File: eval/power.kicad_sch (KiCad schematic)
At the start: 33 parts, among them Q1 BSC0702LS, Q2 BSC0702LS, U2 LM5148RGYR, U3 INA180A3, U8 INA180A3

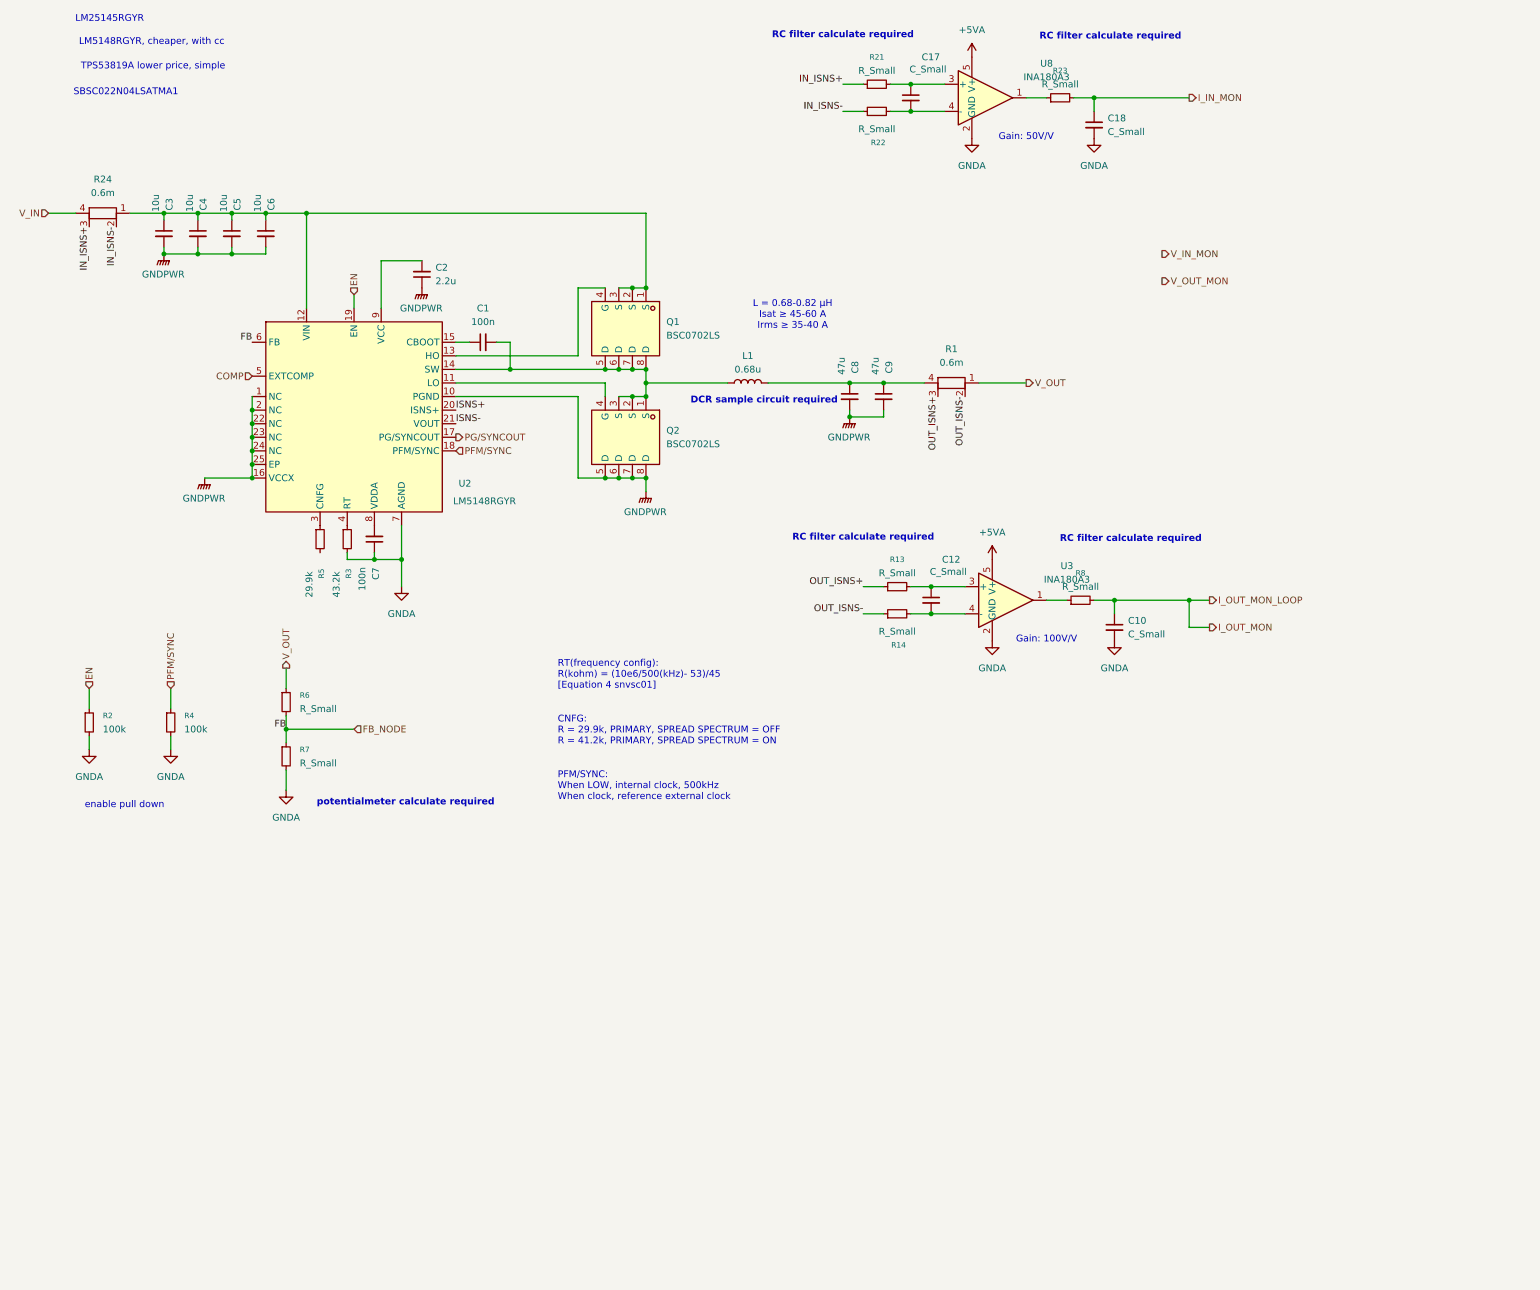
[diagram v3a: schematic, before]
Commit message: Complete first complete draft sch (add screen spi and back light cc)
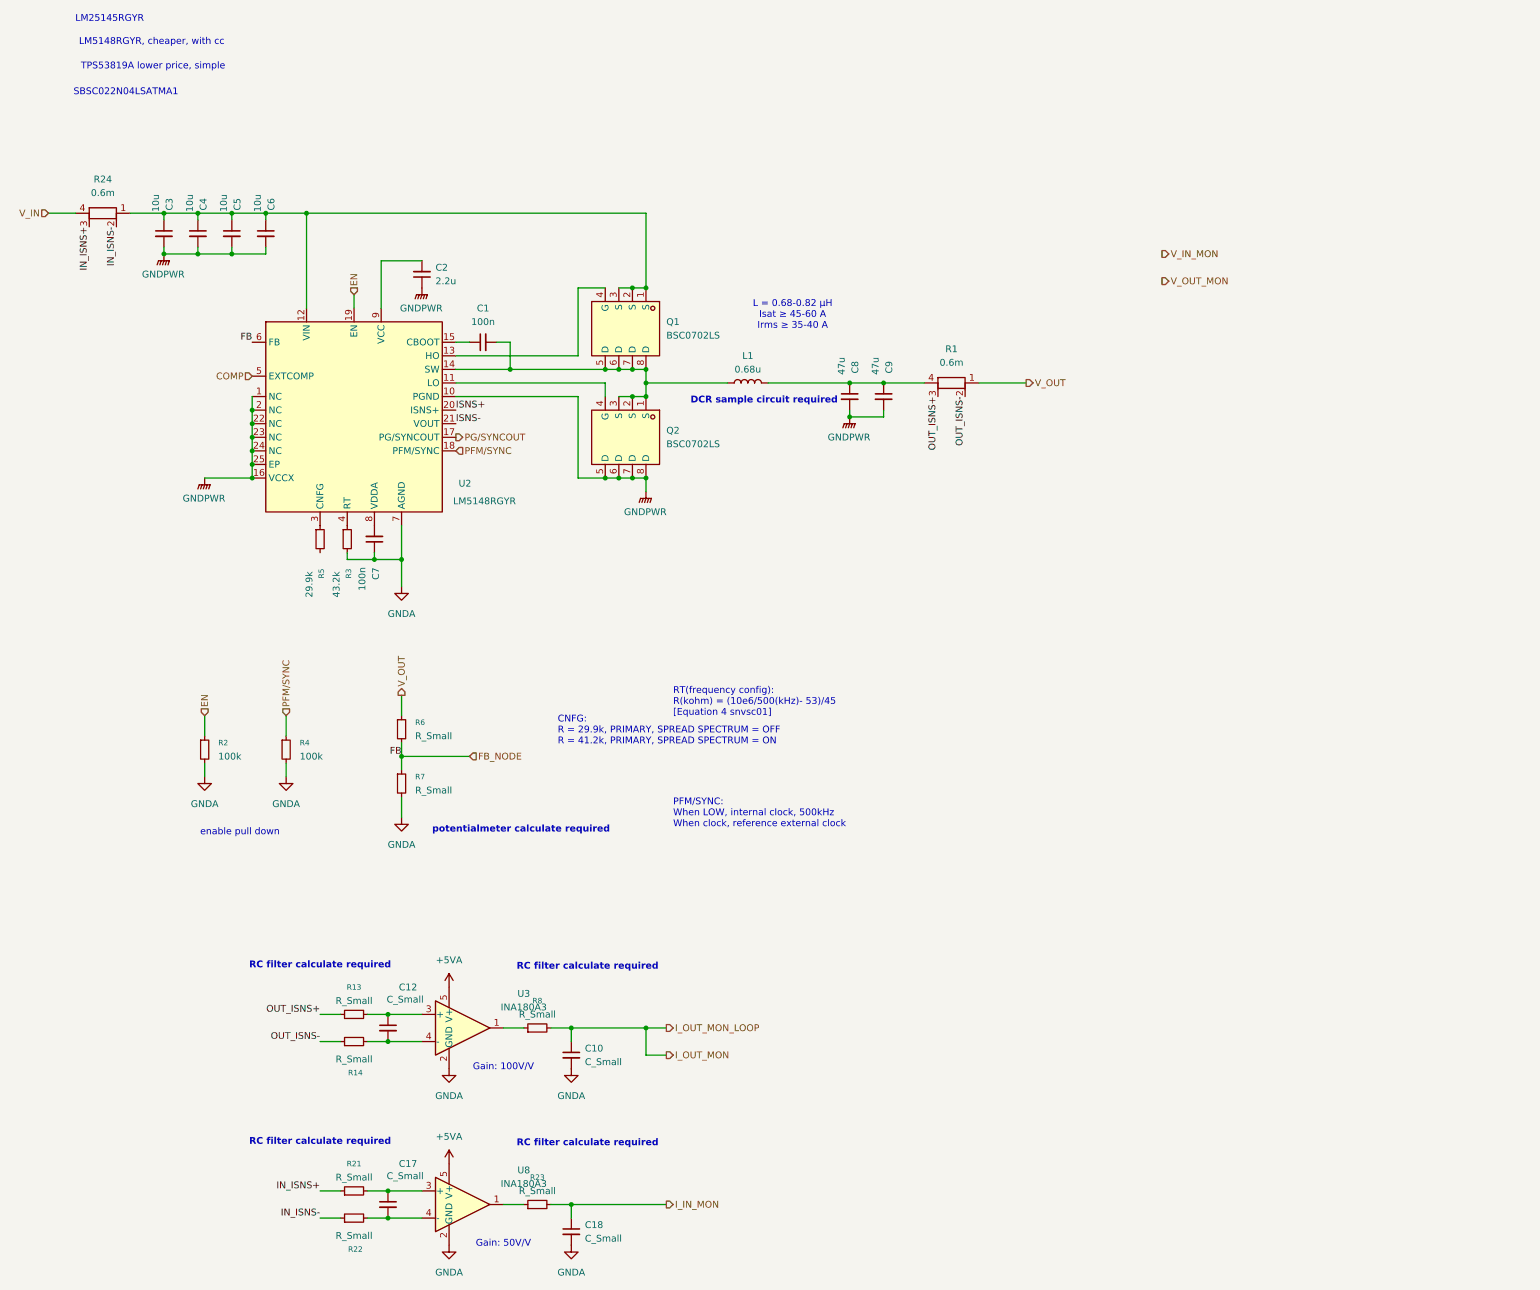
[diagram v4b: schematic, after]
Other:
- moved on the sheet: C10, C12, C17, C18, R13, R14, R2, R21, R22, R23, R4, R6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

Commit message: [Layout] complete loop, root and buck layout
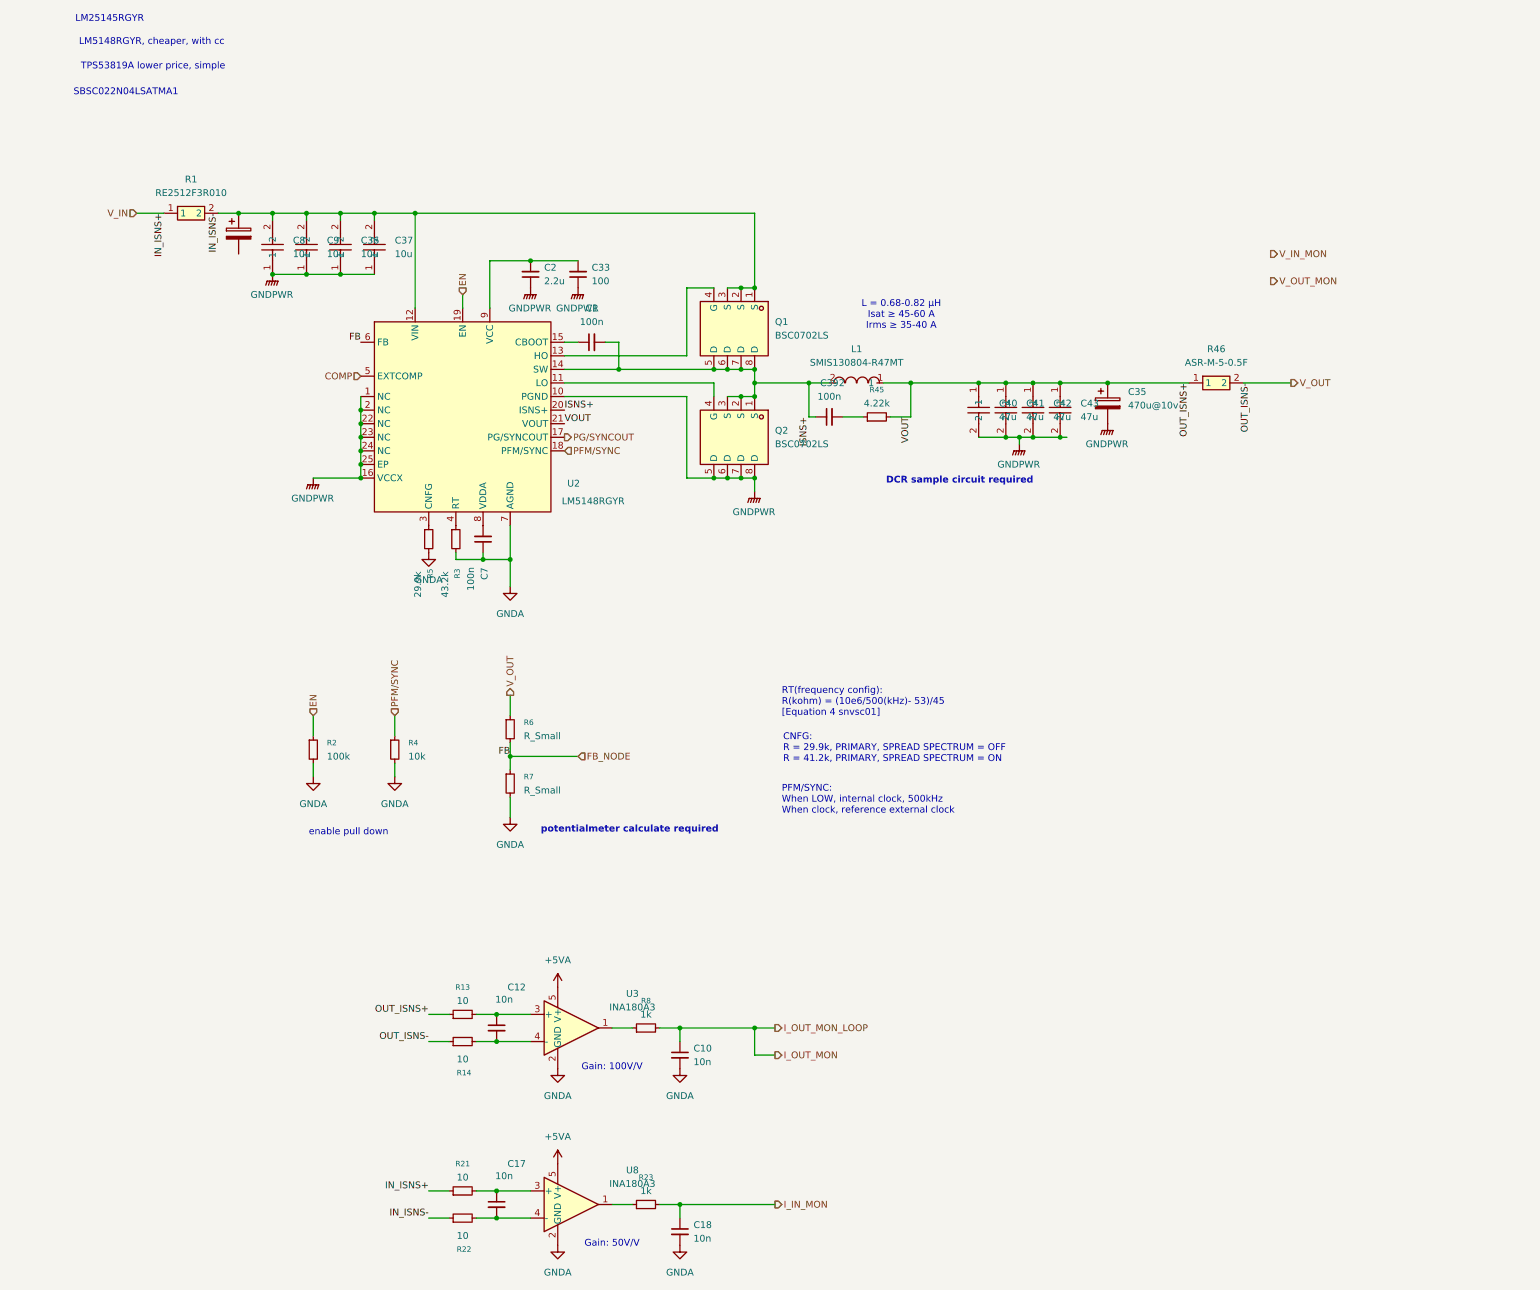
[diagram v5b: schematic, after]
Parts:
- removed C3, C4, C5, C6: 10u, symbol Device:C_Small
- removed C8, C9: 47u, symbol Device:C_Small
- removed L1: 0.68u, symbol Device:L
- removed R1, R24: 0.6m, symbol Device:R_Shunt
- added C33: 100, Capacitor_SMD:C_0603_1608Metric, symbol Device:C_Small
- added C34: 470u@35v, symbol Device:C_Polarized
- added C35: 470u@10v, symbol Device:C_Polarized
- added C36, C37, C8, C9: 10u, EasyEDA:C1206, symbol EasyEDA:HGC1206R5106K500NSPJ
- added C39: 100n, symbol Device:C_Small
- added C40, C41, C42, C43: 47u, EasyEDA:C1206, symbol EasyEDA:HGC1206R5476M100NSPJ
- added L1: SMIS130804-R47MT, EasyEDA:IND-SMD_L12.8-W7.8, symbol EasyEDA:SMIS130804-R47MT
- added R1: RE2512F3R010, EasyEDA:R2512, symbol EasyEDA:RE2512F3R010
- added R45: 4.22k, symbol Device:R_Small
- added R46: ASR-M-5-0.5F, EasyEDA:R3920, symbol EasyEDA:ASR-M-5-0.5F
- C1, C2, C7: footprint (none) -> Capacitor_SMD:C_0603_1608Metric
- C10, C12, C17, C18: value C_Small -> 10n; footprint (none) -> Capacitor_SMD:C_0603_1608Metric
- R13, R14, R21, R22: value R_Small -> 10; footprint (none) -> Resistor_SMD:R_0603_1608Metric
- R2, R3, R5, R6, R7: footprint (none) -> Resistor_SMD:R_0603_1608Metric
- R23, R8: value R_Small -> 1k; footprint (none) -> Resistor_SMD:R_0603_1608Metric
- R4: value 100k -> 10k; footprint (none) -> Resistor_SMD:R_0603_1608Metric
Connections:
- net IN_ISNS+ is gone; now on net V_IN: R21.1
- net ISNS- is gone; now on net OUT_ISNS+: U2.21 (VOUT)
- net OUT_ISNS- is gone; now on net V_OUT: R14.1
- net GNDA: now also R5.2
- net GNDPWR: now also C33.1, C35.2, C36.1, C37.1, C40.2, C41.2, C42.2, C43.2, C8.1, C9.1
- net IN_ISNS-: now also Q1.1 (S), Q1.2 (S), Q1.3 (S), U2.12 (VIN), C34.1, C36.2, C37.2, C8.2, C9.2, R1.2
- net ISNS+: now also C1.2, Q1.5 (D), Q1.6 (D), Q1.7 (D), Q1.8 (D), Q2.1 (S), Q2.2 (S), Q2.3 (S), U2.14 (SW), C39.1, L1.2
- net OUT_ISNS+: now also C35.1, C40.1, C41.1, C42.1, C43.1, L1.1, R45.2, R46.1
- net V_IN: now also R1.1
- net V_OUT: now also R46.2
- net at C2.2, U2.9 (VCC): now also C33.2
- new net: C39.2, R45.1
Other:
- note removed: "RC filter calculate required"
- moved on the sheet: C1, C10, C12, C17, C18, C2, C7, Q1, Q2, R13, R14, R2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

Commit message: [layout] complete for each sub module
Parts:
- C39: footprint (none) -> Capacitor_SMD:C_0603_1608Metric
- R45: footprint (none) -> Resistor_SMD:R_0603_1608Metric
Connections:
- net GNDPWR: now also C34.2
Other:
- moved on the sheet: C36, C37, C8, C9, R1
